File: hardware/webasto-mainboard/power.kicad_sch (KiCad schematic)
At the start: 14 parts, among them U5 BD9G341EFJ

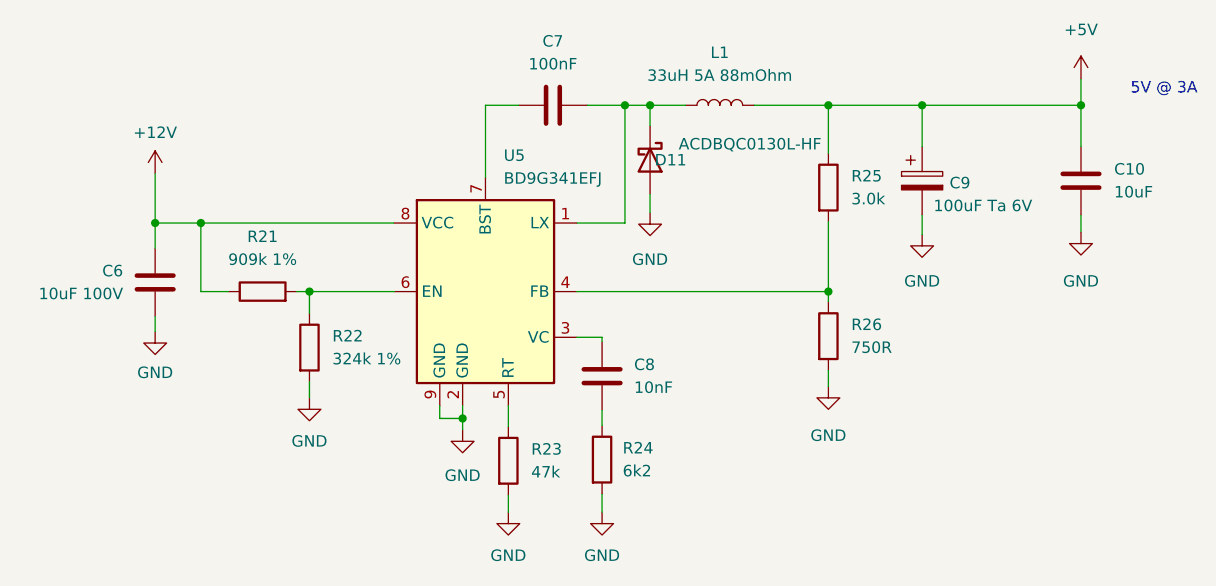
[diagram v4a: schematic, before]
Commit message: Moved emerg. shutdown offboard
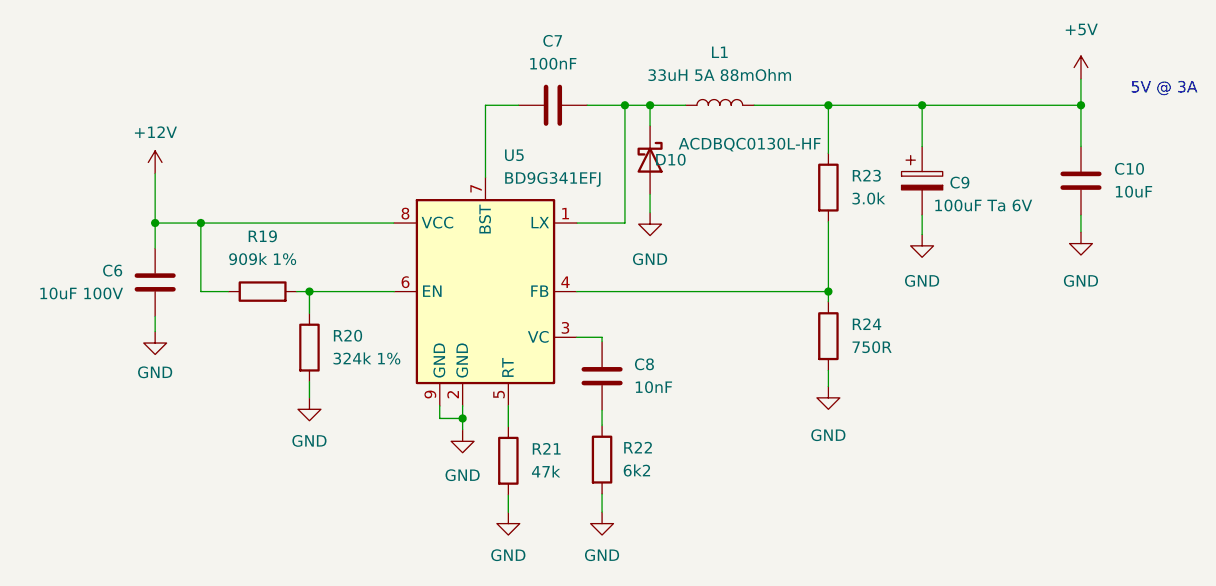
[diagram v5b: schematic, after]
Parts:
- renumbered D11 to D10, R21 to R19, R22 to R20, R23 to R21, R24 to R22, R25 to R23, R26 to R24
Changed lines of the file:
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@@
   (title_block
     (title "Webasto Replacement Mainboard (Thermo Top C)")
-    (date "2023-01-31")
-    (rev "v1.0")
+    (date "2023-02-10")
+    (rev "2.0")
     (company "Gavin Hurlbut")
   )
@@
   (symbol (lib_id "Device:D_Schottky") (at 163.068 65.278 270) (unit 1)
     (in_bom yes) (on_board yes)
-    (property "Reference" "D11" (id 0) (at 167.132 65.278 90)
+    (property "Reference" "D10" (id 0) (at 167.132 65.278 90)
       (effects (font (size 1.27 1.27)) (justify right))
     )
@@
   (symbol (lib_id "Device:R") (at 125.222 86.106 0) (unit 1)
     (in_bom yes) (on_board yes) (fields_autoplaced)
-    (property "Reference" "R22" (id 0) (at 127.762 84.8359 0)
+    (property "Reference" "R20" (id 0) (at 127.762 84.8359 0)
       (effects (font (size 1.27 1.27)) (justify left))
     )
@@
   (symbol (lib_id "power:GND") (at 210.947 73.279 0) (unit 1)
     (in_bom yes) (on_board yes) (fields_autoplaced)
-    (property "Reference" "#PWR063" (id 0) (at 210.947 79.629 0)
+    (property "Reference" "#PWR062" (id 0) (at 210.947 79.629 0)
       (effects (font (size 1.27 1.27)) hide)
     )
@@
   (symbol (lib_id "Device:R") (at 147.32 98.679 0) (unit 1)
     (in_bom yes) (on_board yes) (fields_autoplaced)
-    (property "Reference" "R23" (id 0) (at 149.86 97.4089 0)
+    (property "Reference" "R21" (id 0) (at 149.86 97.4089 0)
       (effects (font (size 1.27 1.27)) (justify left))
     )
@@
   (symbol (lib_id "power:GND") (at 163.068 71.12 0) (unit 1)
     (in_bom yes) (on_board yes) (fields_autoplaced)
-    (property "Reference" "#PWR059" (id 0) (at 163.068 77.47 0)
+    (property "Reference" "#PWR058" (id 0) (at 163.068 77.47 0)
       (effects (font (size 1.27 1.27)) hide)
     )
@@
   (symbol (lib_id "Device:R") (at 182.88 68.326 0) (unit 1)
     (in_bom yes) (on_board yes) (fields_autoplaced)
-    (property "Reference" "R25" (id 0) (at 185.42 67.0559 0)
+    (property "Reference" "R23" (id 0) (at 185.42 67.0559 0)
       (effects (font (size 1.27 1.27)) (justify left))
     )
@@
   (symbol (lib_id "power:GND") (at 193.294 73.533 0) (unit 1)
     (in_bom yes) (on_board yes) (fields_autoplaced)
-    (property "Reference" "#PWR061" (id 0) (at 193.294 79.883 0)
+    (property "Reference" "#PWR060" (id 0) (at 193.294 79.883 0)
       (effects (font (size 1.27 1.27)) hide)
     )
@@
   (symbol (lib_id "Device:R") (at 182.88 84.836 0) (unit 1)
     (in_bom yes) (on_board yes) (fields_autoplaced)
-    (property "Reference" "R26" (id 0) (at 185.42 83.5659 0)
+    (property "Reference" "R24" (id 0) (at 185.42 83.5659 0)
       (effects (font (size 1.27 1.27)) (justify left))
     )
@@
   (symbol (lib_id "power:GND") (at 108.077 84.328 0) (unit 1)
     (in_bom yes) (on_board yes) (fields_autoplaced)
-    (property "Reference" "#PWR054" (id 0) (at 108.077 90.678 0)
+    (property "Reference" "#PWR053" (id 0) (at 108.077 90.678 0)
       (effects (font (size 1.27 1.27)) hide)
     )
@@
   (symbol (lib_id "power:GND") (at 142.24 95.25 0) (unit 1)
     (in_bom yes) (on_board yes) (fields_autoplaced)
-    (property "Reference" "#PWR056" (id 0) (at 142.24 101.6 0)
+    (property "Reference" "#PWR055" (id 0) (at 142.24 101.6 0)
       (effects (font (size 1.27 1.27)) hide)
     )
@@
   (symbol (lib_id "power:GND") (at 125.222 91.694 0) (unit 1)
     (in_bom yes) (on_board yes) (fields_autoplaced)
-    (property "Reference" "#PWR055" (id 0) (at 125.222 98.044 0)
+    (property "Reference" "#PWR054" (id 0) (at 125.222 98.044 0)
       (effects (font (size 1.27 1.27)) hide)
     )
@@
   (symbol (lib_id "power:+12V") (at 108.077 66.802 0) (unit 1)
     (in_bom yes) (on_board yes) (fields_autoplaced)
-    (property "Reference" "#PWR053" (id 0) (at 108.077 70.612 0)
+    (property "Reference" "#PWR052" (id 0) (at 108.077 70.612 0)
       (effects (font (size 1.27 1.27)) hide)
     )
@@
   (symbol (lib_id "power:GND") (at 182.88 90.424 0) (unit 1)
     (in_bom yes) (on_board yes) (fields_autoplaced)
-    (property "Reference" "#PWR060" (id 0) (at 182.88 96.774 0)
+    (property "Reference" "#PWR059" (id 0) (at 182.88 96.774 0)
       (effects (font (size 1.27 1.27)) hide)
     )
@@
   (symbol (lib_id "power:+5V") (at 210.947 56.261 0) (unit 1)
     (in_bom yes) (on_board yes) (fields_autoplaced)
-    (property "Reference" "#PWR062" (id 0) (at 210.947 60.071 0)
+    (property "Reference" "#PWR061" (id 0) (at 210.947 60.071 0)
       (effects (font (size 1.27 1.27)) hide)
     )
@@
   (symbol (lib_id "Device:R") (at 120.015 79.883 90) (unit 1)
     (in_bom yes) (on_board yes) (fields_autoplaced)
-    (property "Reference" "R21" (id 0) (at 120.015 73.787 90))
+    (property "Reference" "R19" (id 0) (at 120.015 73.787 90))
     (property "Value" "909k 1%" (id 1) (at 120.015 76.327 90))
     (property "Footprint" "Resistor_SMD:R_0805_2012Metric_Pad1.20x1.40mm_HandSolder" (id 2) (at 120.015 81.661 90)
@@
   (symbol (lib_id "power:GND") (at 147.32 104.394 0) (unit 1)
     (in_bom yes) (on_board yes) (fields_autoplaced)
-    (property "Reference" "#PWR057" (id 0) (at 147.32 110.744 0)
+    (property "Reference" "#PWR056" (id 0) (at 147.32 110.744 0)
       (effects (font (size 1.27 1.27)) hide)
     )
@@
   (symbol (lib_id "Device:R") (at 157.734 98.552 0) (unit 1)
     (in_bom yes) (on_board yes) (fields_autoplaced)
-    (property "Reference" "R24" (id 0) (at 160.02 97.2819 0)
+    (property "Reference" "R22" (id 0) (at 160.02 97.2819 0)
       (effects (font (size 1.27 1.27)) (justify left))
     )
@@
   (symbol (lib_id "power:GND") (at 157.734 104.394 0) (unit 1)
     (in_bom yes) (on_board yes) (fields_autoplaced)
-    (property "Reference" "#PWR058" (id 0) (at 157.734 110.744 0)
-      (effects (font (size 1.27 1.27)) hide)
-    )
+    (property "Reference" "#PWR057" (id 0) (at 157.734 110.744 0)
+      (effects (font (size 1.27 1.27)) hide)
+    )

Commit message: Got rid of TINY diode (0402!?!?), remove USE_USB, put in PicoW
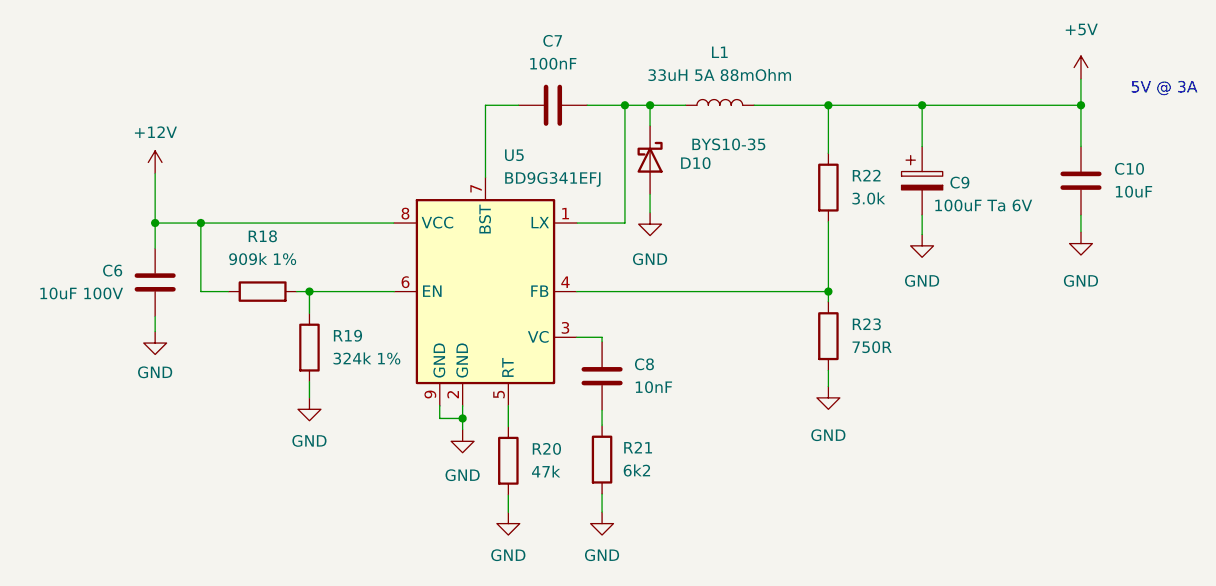
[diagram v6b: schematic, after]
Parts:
- D10: value ACDBQC0130L-HF -> BYS10-35; footprint Diode_SMD:D_SOD-923 -> Diode_SMD:D_SMA_Handsoldering
- renumbered R19 to R18, R20 to R19, R21 to R20, R22 to R21, R23 to R22, R24 to R23
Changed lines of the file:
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@@
   (title_block
     (title "Webasto Replacement Mainboard (Thermo Top C)")
-    (date "2023-02-10")
+    (date "2023-02-14")
     (rev "2.0")
     (company "Gavin Hurlbut")
@@
   (symbol (lib_id "Device:D_Schottky") (at 163.068 65.278 270) (unit 1)
     (in_bom yes) (on_board yes)
-    (property "Reference" "D10" (id 0) (at 167.132 65.278 90)
+    (property "Reference" "D10" (id 0) (at 169.9006 65.659 90)
       (effects (font (size 1.27 1.27)) (justify right))
     )
-    (property "Value" "ACDBQC0130L-HF" (id 1) (at 182.118 63.5 90)
+    (property "Value" "BYS10-35" (id 1) (at 176.022 63.5762 90)
       (effects (font (size 1.27 1.27)) (justify right))
     )
-    (property "Footprint" "Diode_SMD:D_SOD-923" (id 2) (at 163.068 65.278 0)
+    (property "Footprint" "Diode_SMD:D_SMA_Handsoldering" (id 2) (at 163.068 65.278 0)
       (effects (font (size 1.27 1.27)) hide)
     )
@@
   (symbol (lib_id "Device:R") (at 125.222 86.106 0) (unit 1)
     (in_bom yes) (on_board yes) (fields_autoplaced)
-    (property "Reference" "R20" (id 0) (at 127.762 84.8359 0)
+    (property "Reference" "R19" (id 0) (at 127.762 84.8359 0)
       (effects (font (size 1.27 1.27)) (justify left))
     )
@@
   (symbol (lib_id "power:GND") (at 210.947 73.279 0) (unit 1)
     (in_bom yes) (on_board yes) (fields_autoplaced)
-    (property "Reference" "#PWR062" (id 0) (at 210.947 79.629 0)
+    (property "Reference" "#PWR060" (id 0) (at 210.947 79.629 0)
       (effects (font (size 1.27 1.27)) hide)
     )
@@
   (symbol (lib_id "Device:R") (at 147.32 98.679 0) (unit 1)
     (in_bom yes) (on_board yes) (fields_autoplaced)
-    (property "Reference" "R21" (id 0) (at 149.86 97.4089 0)
+    (property "Reference" "R20" (id 0) (at 149.86 97.4089 0)
       (effects (font (size 1.27 1.27)) (justify left))
     )
@@
   (symbol (lib_id "power:GND") (at 163.068 71.12 0) (unit 1)
     (in_bom yes) (on_board yes) (fields_autoplaced)
-    (property "Reference" "#PWR058" (id 0) (at 163.068 77.47 0)
+    (property "Reference" "#PWR056" (id 0) (at 163.068 77.47 0)
       (effects (font (size 1.27 1.27)) hide)
     )
@@
   (symbol (lib_id "Device:R") (at 182.88 68.326 0) (unit 1)
     (in_bom yes) (on_board yes) (fields_autoplaced)
-    (property "Reference" "R23" (id 0) (at 185.42 67.0559 0)
+    (property "Reference" "R22" (id 0) (at 185.42 67.0559 0)
       (effects (font (size 1.27 1.27)) (justify left))
     )
@@
   (symbol (lib_id "power:GND") (at 193.294 73.533 0) (unit 1)
     (in_bom yes) (on_board yes) (fields_autoplaced)
-    (property "Reference" "#PWR060" (id 0) (at 193.294 79.883 0)
+    (property "Reference" "#PWR058" (id 0) (at 193.294 79.883 0)
       (effects (font (size 1.27 1.27)) hide)
     )
@@
   (symbol (lib_id "Device:R") (at 182.88 84.836 0) (unit 1)
     (in_bom yes) (on_board yes) (fields_autoplaced)
-    (property "Reference" "R24" (id 0) (at 185.42 83.5659 0)
+    (property "Reference" "R23" (id 0) (at 185.42 83.5659 0)
       (effects (font (size 1.27 1.27)) (justify left))
     )
@@
   (symbol (lib_id "power:GND") (at 108.077 84.328 0) (unit 1)
     (in_bom yes) (on_board yes) (fields_autoplaced)
-    (property "Reference" "#PWR053" (id 0) (at 108.077 90.678 0)
+    (property "Reference" "#PWR051" (id 0) (at 108.077 90.678 0)
       (effects (font (size 1.27 1.27)) hide)
     )
@@
   (symbol (lib_id "power:GND") (at 142.24 95.25 0) (unit 1)
     (in_bom yes) (on_board yes) (fields_autoplaced)
-    (property "Reference" "#PWR055" (id 0) (at 142.24 101.6 0)
+    (property "Reference" "#PWR053" (id 0) (at 142.24 101.6 0)
       (effects (font (size 1.27 1.27)) hide)
     )
@@
   (symbol (lib_id "power:GND") (at 125.222 91.694 0) (unit 1)
     (in_bom yes) (on_board yes) (fields_autoplaced)
-    (property "Reference" "#PWR054" (id 0) (at 125.222 98.044 0)
+    (property "Reference" "#PWR052" (id 0) (at 125.222 98.044 0)
       (effects (font (size 1.27 1.27)) hide)
     )
@@
   (symbol (lib_id "power:+12V") (at 108.077 66.802 0) (unit 1)
     (in_bom yes) (on_board yes) (fields_autoplaced)
-    (property "Reference" "#PWR052" (id 0) (at 108.077 70.612 0)
+    (property "Reference" "#PWR050" (id 0) (at 108.077 70.612 0)
       (effects (font (size 1.27 1.27)) hide)
     )
@@
   (symbol (lib_id "power:GND") (at 182.88 90.424 0) (unit 1)
     (in_bom yes) (on_board yes) (fields_autoplaced)
-    (property "Reference" "#PWR059" (id 0) (at 182.88 96.774 0)
+    (property "Reference" "#PWR057" (id 0) (at 182.88 96.774 0)
       (effects (font (size 1.27 1.27)) hide)
     )
@@
   (symbol (lib_id "power:+5V") (at 210.947 56.261 0) (unit 1)
     (in_bom yes) (on_board yes) (fields_autoplaced)
-    (property "Reference" "#PWR061" (id 0) (at 210.947 60.071 0)
+    (property "Reference" "#PWR059" (id 0) (at 210.947 60.071 0)
       (effects (font (size 1.27 1.27)) hide)
     )
@@
   (symbol (lib_id "Device:R") (at 120.015 79.883 90) (unit 1)
     (in_bom yes) (on_board yes) (fields_autoplaced)
-    (property "Reference" "R19" (id 0) (at 120.015 73.787 90))
+    (property "Reference" "R18" (id 0) (at 120.015 73.787 90))
     (property "Value" "909k 1%" (id 1) (at 120.015 76.327 90))
     (property "Footprint" "Resistor_SMD:R_0805_2012Metric_Pad1.20x1.40mm_HandSolder" (id 2) (at 120.015 81.661 90)
@@
   (symbol (lib_id "power:GND") (at 147.32 104.394 0) (unit 1)
     (in_bom yes) (on_board yes) (fields_autoplaced)
-    (property "Reference" "#PWR056" (id 0) (at 147.32 110.744 0)
+    (property "Reference" "#PWR054" (id 0) (at 147.32 110.744 0)
       (effects (font (size 1.27 1.27)) hide)
     )
@@
   (symbol (lib_id "Device:R") (at 157.734 98.552 0) (unit 1)
     (in_bom yes) (on_board yes) (fields_autoplaced)
-    (property "Reference" "R22" (id 0) (at 160.02 97.2819 0)
+    (property "Reference" "R21" (id 0) (at 160.02 97.2819 0)
       (effects (font (size 1.27 1.27)) (justify left))
     )
@@
   (symbol (lib_id "power:GND") (at 157.734 104.394 0) (unit 1)
     (in_bom yes) (on_board yes) (fields_autoplaced)
-    (property "Reference" "#PWR057" (id 0) (at 157.734 110.744 0)
-      (effects (font (size 1.27 1.27)) hide)
-    )
+    (property "Reference" "#PWR055" (id 0) (at 157.734 110.744 0)
+      (effects (font (size 1.27 1.27)) hide)
+    )

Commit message: Move VSYS to ADC2 to avoid the stupid WiFi setup
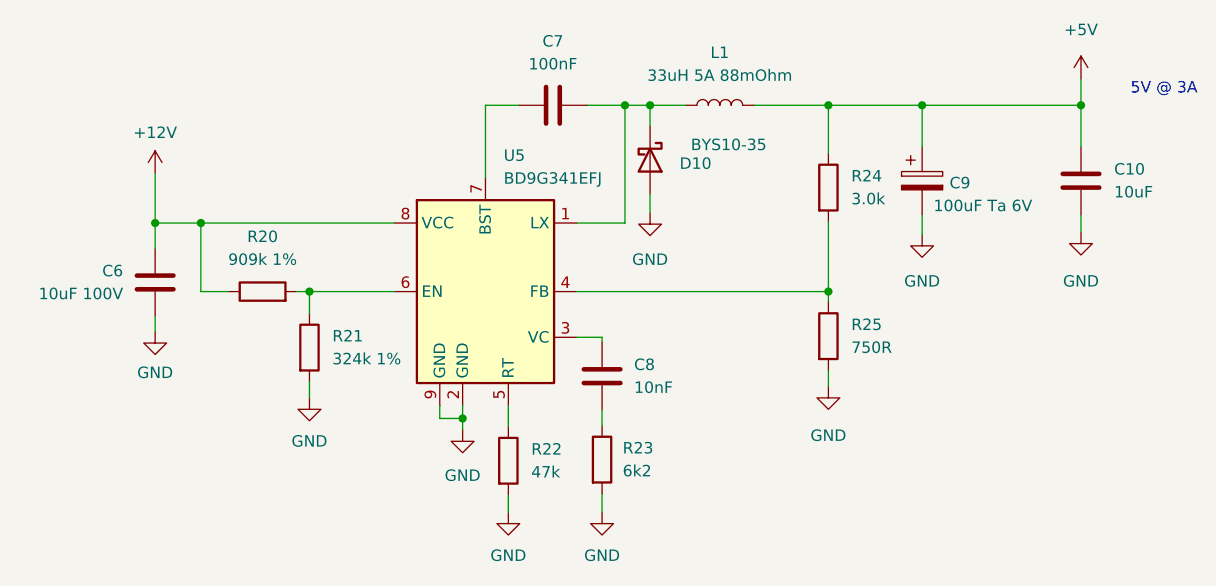
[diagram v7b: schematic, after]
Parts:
- renumbered R18 to R20, R19 to R21, R20 to R22, R21 to R23, R22 to R24, R23 to R25
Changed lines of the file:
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@@
   (title_block
     (title "Webasto Replacement Mainboard (Thermo Top C)")
-    (date "2023-02-14")
+    (date "2023-02-22")
     (rev "2.0")
     (company "Gavin Hurlbut")
@@
   (symbol (lib_id "Device:R") (at 125.222 86.106 0) (unit 1)
     (in_bom yes) (on_board yes) (fields_autoplaced)
-    (property "Reference" "R19" (id 0) (at 127.762 84.8359 0)
+    (property "Reference" "R21" (id 0) (at 127.762 84.8359 0)
       (effects (font (size 1.27 1.27)) (justify left))
     )
@@
   (symbol (lib_id "Device:R") (at 147.32 98.679 0) (unit 1)
     (in_bom yes) (on_board yes) (fields_autoplaced)
-    (property "Reference" "R20" (id 0) (at 149.86 97.4089 0)
+    (property "Reference" "R22" (id 0) (at 149.86 97.4089 0)
       (effects (font (size 1.27 1.27)) (justify left))
     )
@@
   (symbol (lib_id "Device:R") (at 182.88 68.326 0) (unit 1)
     (in_bom yes) (on_board yes) (fields_autoplaced)
-    (property "Reference" "R22" (id 0) (at 185.42 67.0559 0)
+    (property "Reference" "R24" (id 0) (at 185.42 67.0559 0)
       (effects (font (size 1.27 1.27)) (justify left))
     )
@@
   (symbol (lib_id "Device:R") (at 182.88 84.836 0) (unit 1)
     (in_bom yes) (on_board yes) (fields_autoplaced)
-    (property "Reference" "R23" (id 0) (at 185.42 83.5659 0)
+    (property "Reference" "R25" (id 0) (at 185.42 83.5659 0)
       (effects (font (size 1.27 1.27)) (justify left))
     )
@@
   (symbol (lib_id "Device:R") (at 120.015 79.883 90) (unit 1)
     (in_bom yes) (on_board yes) (fields_autoplaced)
-    (property "Reference" "R18" (id 0) (at 120.015 73.787 90))
+    (property "Reference" "R20" (id 0) (at 120.015 73.787 90))
     (property "Value" "909k 1%" (id 1) (at 120.015 76.327 90))
     (property "Footprint" "Resistor_SMD:R_0805_2012Metric_Pad1.20x1.40mm_HandSolder" (id 2) (at 120.015 81.661 90)
@@
   (symbol (lib_id "Device:R") (at 157.734 98.552 0) (unit 1)
     (in_bom yes) (on_board yes) (fields_autoplaced)
-    (property "Reference" "R21" (id 0) (at 160.02 97.2819 0)
-      (effects (font (size 1.27 1.27)) (justify left))
-    )
+    (property "Reference" "R23" (id 0) (at 160.02 97.2819 0)
+      (effects (font (size 1.27 1.27)) (justify left))
+    )
